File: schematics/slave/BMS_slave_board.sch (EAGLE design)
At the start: 44 parts, among them Q1 BUZ10, Q2 BUZ10, Q3 BUZ10, Q4 BUZ10, U1 LMV324, U2 LMV324

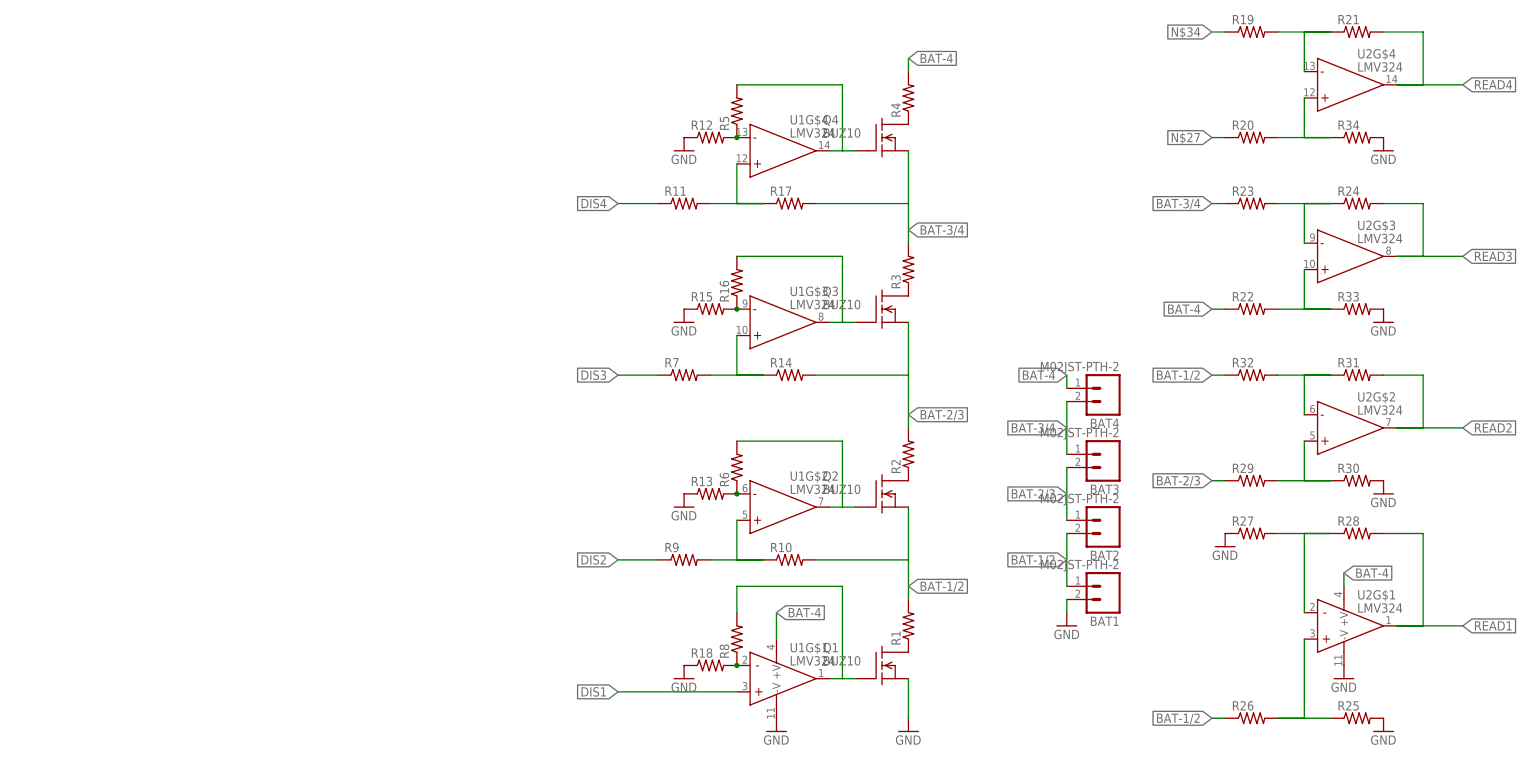
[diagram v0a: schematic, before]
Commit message: Added microcontroller and cleanded analog work
Added the Attiny261, ISP header, linear regulator (and associated
discretes)
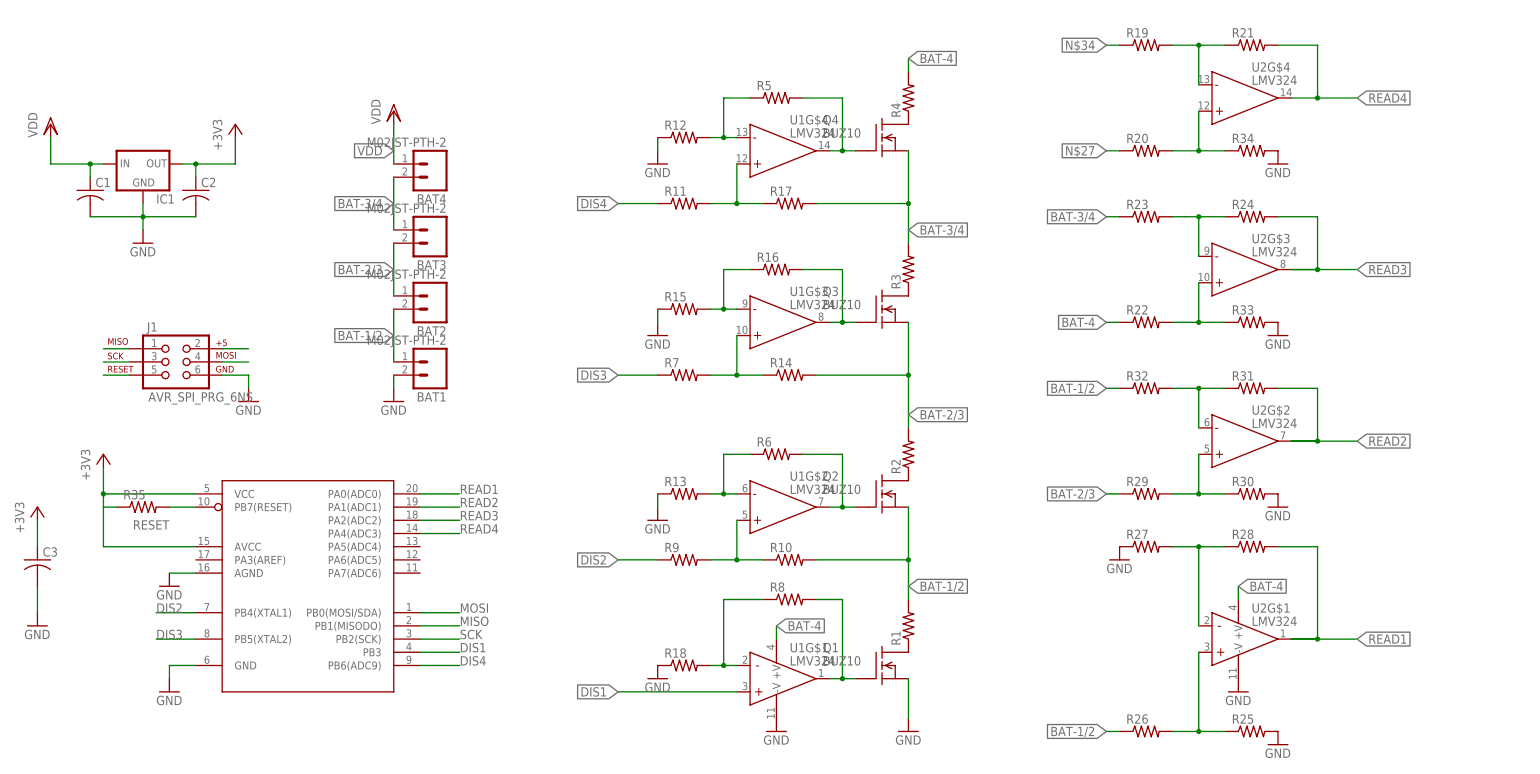
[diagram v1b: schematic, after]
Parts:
- added C1, C2, C3: (no value), resistor:C-US025-024X044
- added IC1: (no value), v-reg:78LXX
- added J1: AVR_SPI_PRG_6NS, SparkFun-Connectors:AVR_SPI_PRG_6NS
- added R35: (no value), rcl:R-US_0204/7
- added U$1: ATTINY261ADIP, EVT-Eagle-Library:ATTINY261ADIP
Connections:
- net N$10 renamed DELDEL
- new net +3V3: C2.1, C3.1, IC1.OUT, R35.1, U$1.AVCC, U$1.VCC
- new net MISO: J1.1, U$1.PB1(MISODO)
- new net MOSI: J1.4, U$1.PB0(MOSI/SDA)
- new net N$26: J1.2
- new net RESET: J1.5, R35.2, U$1.PB7(RESET)
- new net SCK: J1.3, U$1.PB2(SCK)
- new net VDD: BAT4.1, C1.1, IC1.IN
- net BAT-4: no longer BAT4.1
- net DIS1: now also U$1.PB3
- net DIS2: now also U$1.PB4(XTAL1)
- net DIS3: now also U$1.PB5(XTAL2)
- net DIS4: now also U$1.PB6(ADC9)
- net GND: now also C1.2, C2.2, C3.2, IC1.GND, J1.6, U$1.AGND, U$1.GND
- net READ1: now also U$1.PA0(ADC0)
- net READ2: now also U$1.PA1(ADC1)
- net READ3: now also U$1.PA2(ADC2)
- net READ4: now also U$1.PA4(ADC3)
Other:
- moved on the sheet: BAT1, BAT2, BAT3, BAT4, R12, R13, R15, R16, R18, R19, R20, R21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

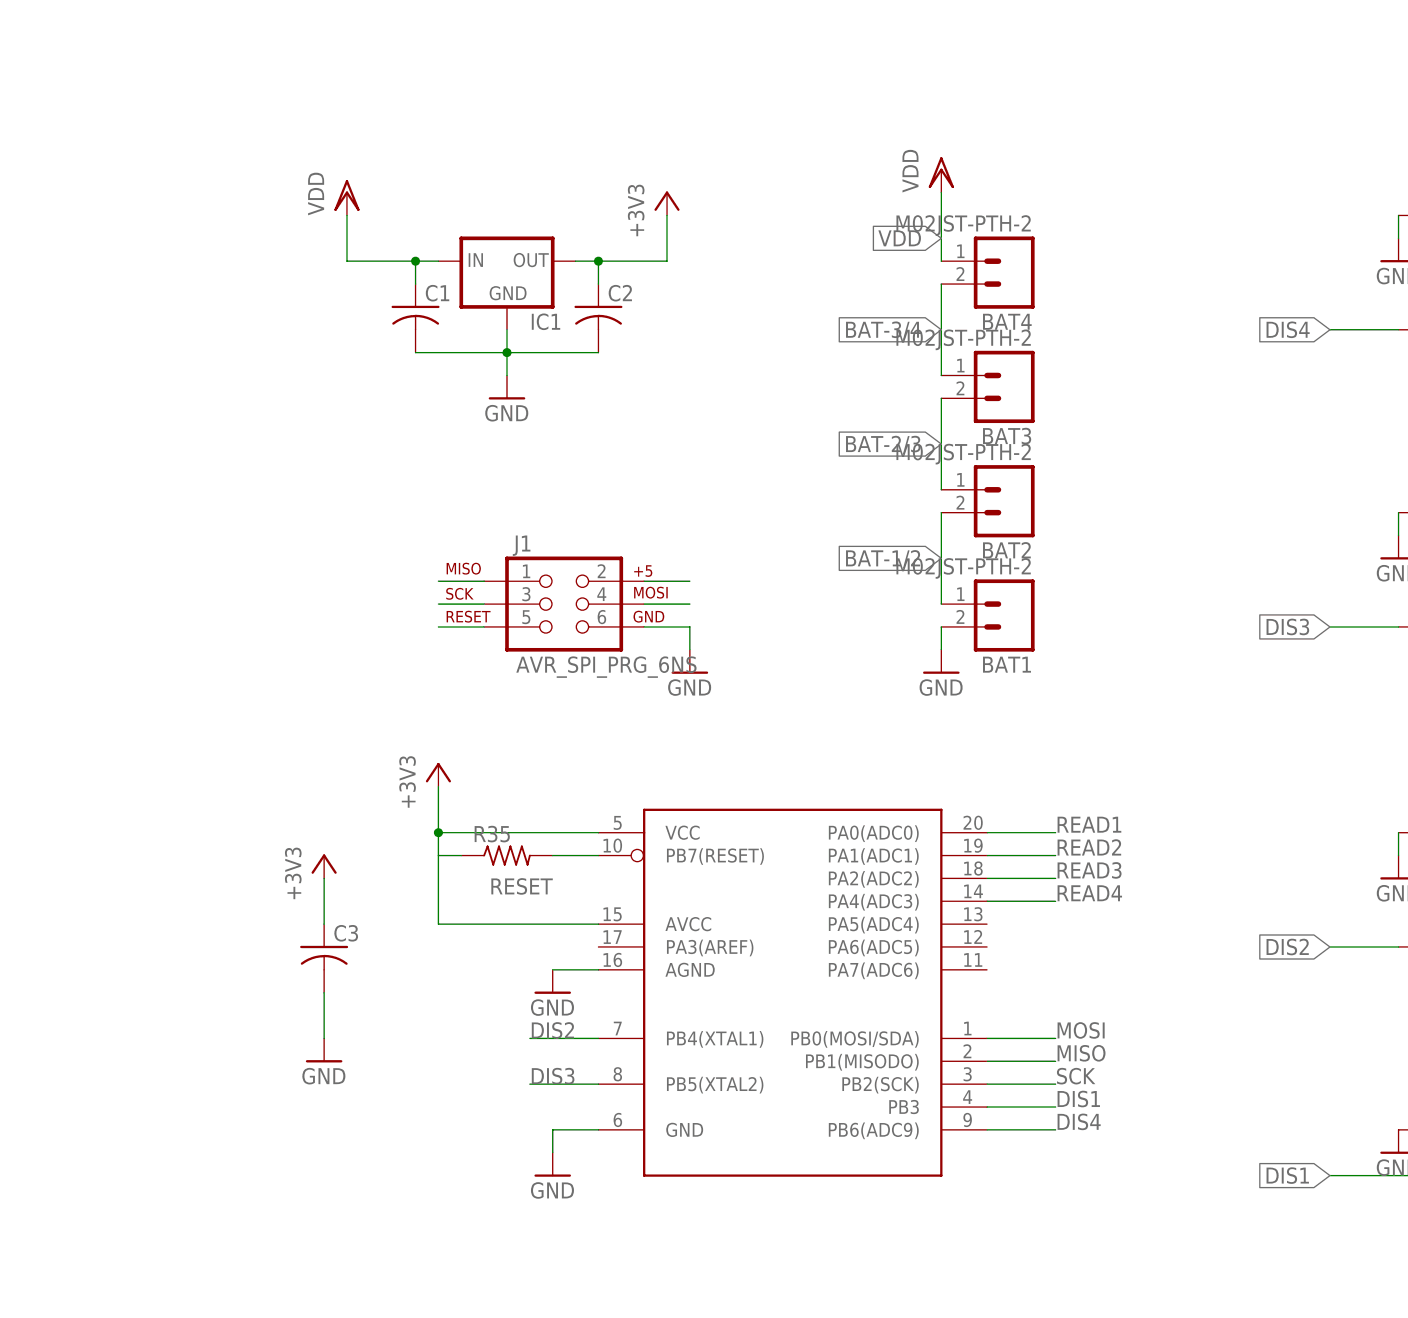
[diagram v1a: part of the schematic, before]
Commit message: added voltage regulator and new uC symbol
also added decoupling caps for analog power supply and cleaned up wiring
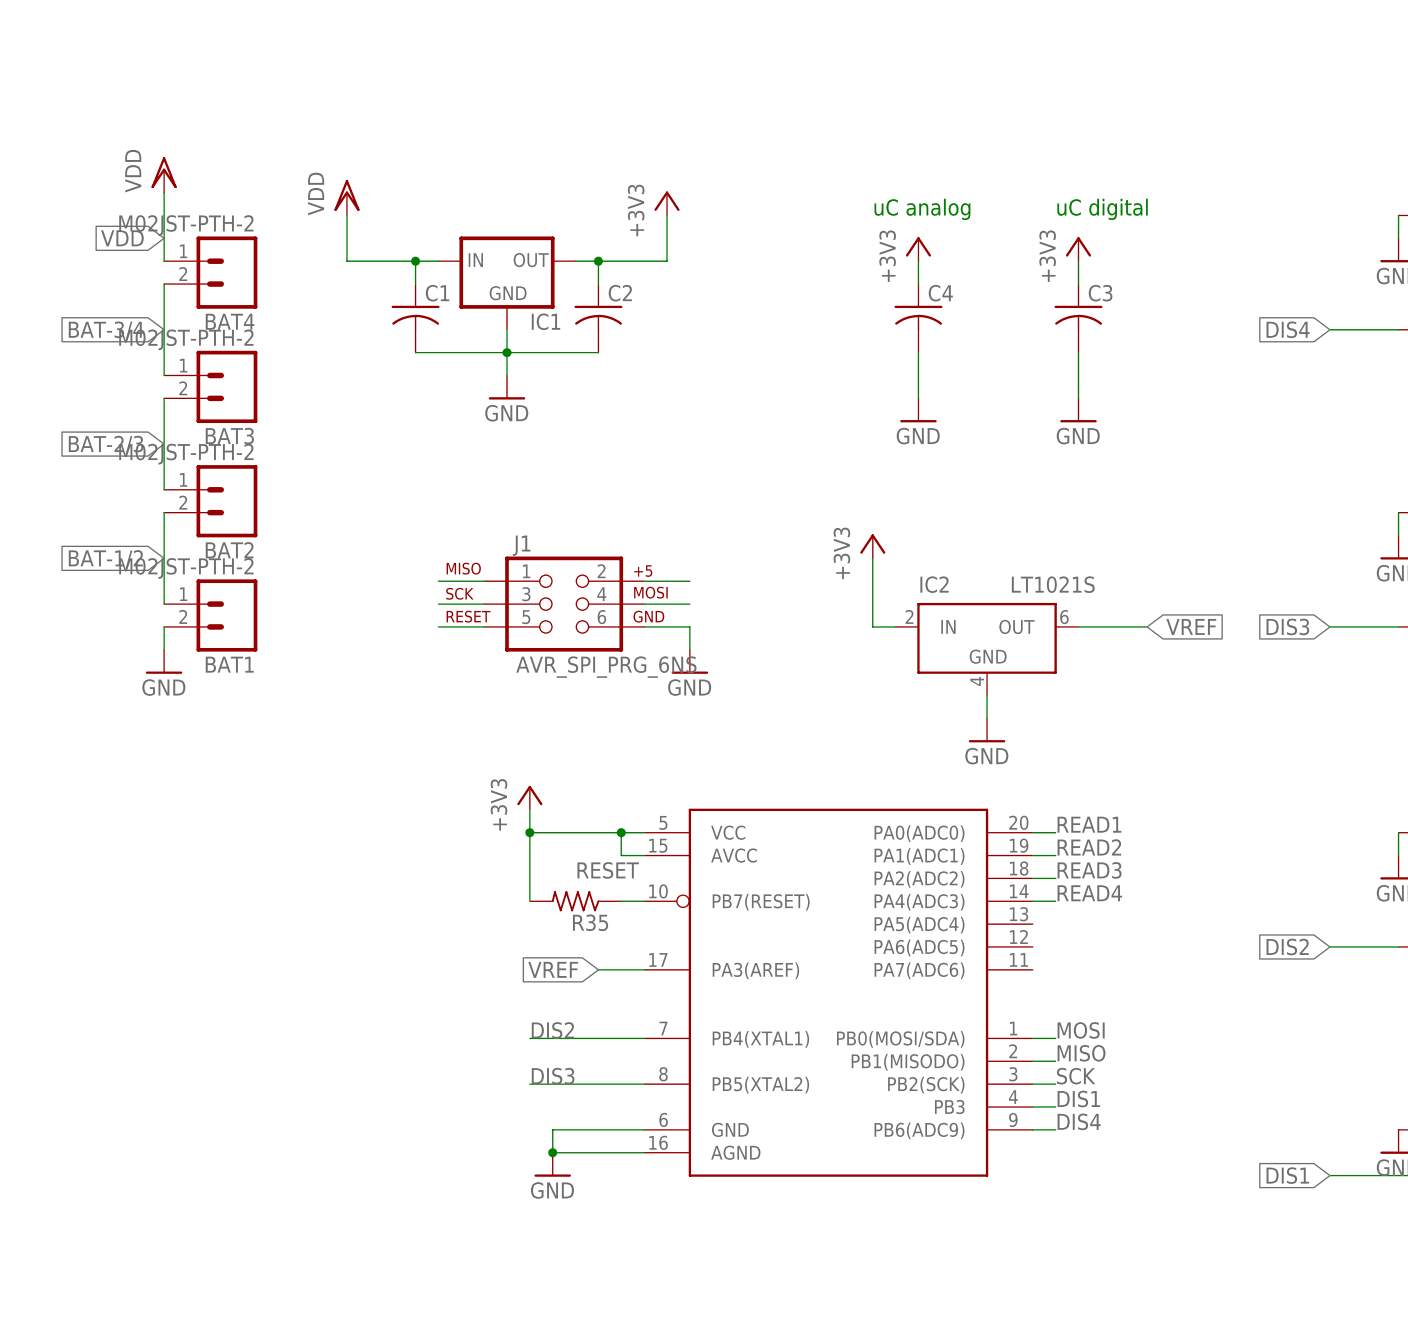
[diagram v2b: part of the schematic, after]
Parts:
- added C4: (no value), resistor:C-US025-024X044
- added IC2: LT1021S, linear-technology:LT1021S
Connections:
- new net VREF: IC2.OUT, U$1.PA3(AREF)
- net +3V3: now also C4.1, IC2.IN, R35.2; no longer R35.1
- net GND: now also C4.2, IC2.GND
- net RESET: now also R35.1; no longer R35.2
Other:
- note added: "uC analog"
- note added: "uC digital"
- moved on the sheet: BAT1, BAT2, BAT3, BAT4, C3, R35
